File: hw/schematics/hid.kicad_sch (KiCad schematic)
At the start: 106 parts, among them M1 SK8701-01-004-SENSOR, SW1 SW_Push, SW10 SW_Push, SW11 SW_Push, SW12 SW_Push, SW13 SW_Push, SW14 SW_Push, SW15 SW_Push, SW16 SW_Push, SW17 SW_Push, SW18 SW_Push, SW19 SW_Push, SW2 SW_Push, SW20 SW_Push, SW21 SW_Push, SW22 SW_Push, SW23 SW_Push, SW3 SW_Push, SW4 SW_Push, SW5 SW_Push, SW6 SW_Push, SW7 SW_Push, SW8 SW_Push, SW9 SW_Push, U3 ADS122S14

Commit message: Hook up matrix
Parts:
- removed M1, rM1: SK8701-01-004-SENSOR, Alidade:SK8707-01-SENSOR, symbol Alidade:SK8701-01-004-SENSOR
- added M1, rM2: SK8701-01-005-SENSOR, Alidade:SK8707-01-005-SENSOR, symbol Alidade:SK8701-01-005-SENSOR
- added R6, R7, R8, R9, rR6, rR7, rR8, rR9: 10k, symbol Alidade:R
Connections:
- net 1V8: now also R6.1, R7.1, R8.1, R9.1
- net AIN0: now also M1.B
- net AIN1: now also M1.A
- net REFN: now also M1.D
- net REFP: now also M1.C
- net r1V8: now also rR6.1, rR7.1, rR8.1, rR9.1
- net rAIN0: now also rM2.B
- net rAIN1: now also rM2.A
- net rREFN: now also rM2.D
- net rREFP: now also rM2.C
- net rCOL2: now reaches rD1.3 (K), rD2.3 (K), rD3.3 (K), rD4.3 (K)
- net rROW2: now reaches rSW11.1, rSW14.1, rSW17.1, rSW20.1, rSW22.2, rSW3.1, rSW6.1
- net rROW2: now also rR7.2
- net COL3: now reaches D5.3 (K), D6.3 (K), D7.3 (K), D8.3 (K)
- net rROW1: now reaches rSW12.1, rSW13.1, rSW18.1, rSW19.1, rSW4.1, rSW5.1
- net rROW1: now also rR6.2
- net ROW3: now reaches SW10.1, SW15.1, SW16.1, SW2.1, SW21.1, SW23.2, SW7.1
- net ROW3: now also R8.2
- net COL6: now reaches D16.3 (K), D17.3 (K), D18.3 (K)
- net COL5: now reaches D13.3 (K), D14.3 (K), D15.3 (K)
- net rCOL6: now reaches rD16.3 (K), rD17.3 (K), rD18.3 (K)
- net rCOL7: now reaches rD19.3 (K), rD20.3 (K), rD21.3 (K)
- net ROW4: now reaches SW1.1, SW8.1, SW9.1
- net ROW4: now also R9.2
- net rCOL3: now reaches rD5.3 (K), rD6.3 (K), rD7.3 (K), rD8.3 (K)
- net rCOL5: now reaches rD13.3 (K), rD14.3 (K), rD15.3 (K)
- net rROW3: now reaches rSW10.1, rSW15.1, rSW16.1, rSW2.1, rSW21.1, rSW23.2, rSW7.1
- net rROW3: now also rR8.2
- net ROW1: now reaches SW12.1, SW13.1, SW18.1, SW19.1, SW4.1, SW5.1
- net ROW1: now also R6.2
- net rCOL4: now reaches rD10.3 (K), rD11.3 (K), rD12.3 (K), rD9.3 (K)
- net rROW4: now reaches rSW1.1, rSW8.1, rSW9.1
- net rROW4: now also rR9.2
- net COL2: now reaches D1.3 (K), D2.3 (K), D3.3 (K), D4.3 (K)
- net ROW2: now reaches SW11.1, SW14.1, SW17.1, SW20.1, SW22.2, SW3.1, SW6.1
- net ROW2: now also R7.2
- net COL1: now reaches D22.3 (K), D23.3 (K)
- net COL4: now reaches D10.3 (K), D11.3 (K), D12.3 (K), D9.3 (K)
- net COL7: now reaches D19.3 (K), D20.3 (K), D21.3 (K)
- net rCOL1: now reaches rD22.3 (K), rD23.3 (K)
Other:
- note added: "To scan the matrix: - Pull row low - Read column"
- note removed: "To scan the matrix: - Pull column low - Read row nibble"

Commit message: Annotate; Remove unused LDO/LS; Add RGB LED to PMIC
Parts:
- renumbered C12 to C10, C13 to C9, R3 to R10, R5 to R11, rC15 to rC10, rC13 to rC9, rR3 to rR10, rR5 to rR11
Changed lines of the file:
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@@
 		(on_board yes)
 		(dnp no)
-		(property "Reference" "rC15"
+		(property "Reference" "rC10"
 			(at 159.766 217.678 0)
 			(effects
@@
 			(project "alidade"
 				(path "/4cc5d416-57f5-4147-8183-e03ae6b1198a/2e72dd0e-817e-4022-b409-1f79b0de6857"
-					(reference "rC15")
+					(reference "rC10")
 					(unit 1)
 				)
@@
 		(on_board yes)
 		(dnp no)
-		(property "Reference" "C12"
+		(property "Reference" "C10"
 			(at 35.306 215.138 0)
 			(effects
@@
 			(project "alidade"
 				(path "/4cc5d416-57f5-4147-8183-e03ae6b1198a/2e72dd0e-817e-4022-b409-1f79b0de6857"
-					(reference "C12")
+					(reference "C10")
 					(unit 1)
 				)
@@
 		(on_board yes)
 		(dnp no)
-		(property "Reference" "rC13"
+		(property "Reference" "rC9"
 			(at 150.876 217.678 0)
 			(effects
@@
 			(project "alidade"
 				(path "/4cc5d416-57f5-4147-8183-e03ae6b1198a/2e72dd0e-817e-4022-b409-1f79b0de6857"
-					(reference "rC13")
+					(reference "rC9")
 					(unit 1)
 				)
@@
 		(on_board yes)
 		(dnp no)
-		(property "Reference" "R3"
+		(property "Reference" "R10"
 			(at 77.724 246.38 0)
 			(effects
@@
 			(project ""
 				(path "/4cc5d416-57f5-4147-8183-e03ae6b1198a/2e72dd0e-817e-4022-b409-1f79b0de6857"
-					(reference "R3")
+					(reference "R10")
 					(unit 1)
 				)
@@
 		(on_board yes)
 		(dnp no)
-		(property "Reference" "rR3"
+		(property "Reference" "rR10"
 			(at 202.184 248.92 0)
 			(effects
@@
 			(project "alidade"
 				(path "/4cc5d416-57f5-4147-8183-e03ae6b1198a/2e72dd0e-817e-4022-b409-1f79b0de6857"
-					(reference "rR3")
+					(reference "rR10")
 					(unit 1)
 				)
@@
 		(on_board yes)
 		(dnp no)
-		(property "Reference" "C13"
+		(property "Reference" "C9"
 			(at 26.416 215.138 0)
 			(effects
@@
 			(project "alidade"
 				(path "/4cc5d416-57f5-4147-8183-e03ae6b1198a/2e72dd0e-817e-4022-b409-1f79b0de6857"
-					(reference "C13")
+					(reference "C9")
 					(unit 1)
 				)
@@
 		(on_board yes)
 		(dnp no)
-		(property "Reference" "R5"
+		(property "Reference" "R11"
 			(at 77.724 254 0)
 			(effects
@@
 			(project "alidade"
 				(path "/4cc5d416-57f5-4147-8183-e03ae6b1198a/2e72dd0e-817e-4022-b409-1f79b0de6857"
-					(reference "R5")
+					(reference "R11")
 					(unit 1)
 				)
@@
 		(on_board yes)
 		(dnp no)
-		(property "Reference" "rR5"
+		(property "Reference" "rR11"
 			(at 202.184 256.54 0)
 			(effects
@@
 			(project "alidade"
 				(path "/4cc5d416-57f5-4147-8183-e03ae6b1198a/2e72dd0e-817e-4022-b409-1f79b0de6857"
-					(reference "rR5")
+					(reference "rR11")
 					(unit 1)
 				)

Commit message: Place shphld switches
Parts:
- added SW24, rSW24: SW_Push, symbol Alidade:SW_Push
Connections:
- net GND: now also SW24.2
- net rGND: now also rSW24.2
- new net SHPHLD: SW24.1
- new net rSHPHLD: rSW24.1
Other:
- note added: "SHPHLD Switches"

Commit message: Rename power rails
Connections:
- net 1V8 renamed DVDD
- net 3V3 renamed AVDD
- net r1V8 renamed rDVDD
- net r3V3 renamed rAVDD
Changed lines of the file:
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@@
 	)
 	(symbol
-		(lib_id "Alidade:1V8")
+		(lib_id "Alidade:DVDD")
 		(at 46.99 68.58 0)
 		(unit 1)
@@
 		(dnp no)
 		(fields_autoplaced yes)
-		(property "Reference" "#1V8_011"
+		(property "Reference" "#DVDD0106"
 			(at 46.99 72.39 0)
 			(effects
@@
 			)
 		)
-		(property "Value" "1V8"
+		(property "Value" "DVDD"
 			(at 46.99 63.5 0)
 			(effects
@@
 			(project "alidade"
 				(path "/4cc5d416-57f5-4147-8183-e03ae6b1198a/2e72dd0e-817e-4022-b409-1f79b0de6857"
-					(reference "#1V8_011")
+					(reference "#DVDD0106")
 					(unit 1)
 				)
@@
 	)
 	(symbol
-		(lib_id "Alidade:r3V3")
+		(lib_id "Alidade:rAVDD")
 		(at 158.75 207.01 0)
 		(unit 1)
@@
 		(dnp no)
 		(fields_autoplaced yes)
-		(property "Reference" "#r3V3_02"
+		(property "Reference" "#rAVDD0102"
 			(at 158.75 210.82 0)
 			(effects
@@
 			)
 		)
-		(property "Value" "r3V3"
+		(property "Value" "rAVDD"
 			(at 158.75 201.93 0)
 			(effects
@@
 			(project ""
 				(path "/4cc5d416-57f5-4147-8183-e03ae6b1198a/2e72dd0e-817e-4022-b409-1f79b0de6857"
-					(reference "#r3V3_02")
+					(reference "#rAVDD0102")
 					(unit 1)
 				)
@@
 	)
 	(symbol
-		(lib_id "Alidade:r1V8")
+		(lib_id "Alidade:rDVDD")
 		(at 374.65 99.06 0)
 		(unit 1)
@@
 		(dnp no)
 		(fields_autoplaced yes)
-		(property "Reference" "#r1V8_09"
+		(property "Reference" "#rDVDD0106"
 			(at 374.65 102.87 0)
 			(effects
@@
 			)
 		)
-		(property "Value" "r1V8"
+		(property "Value" "rDVDD"
 			(at 374.65 93.98 0)
 			(effects
@@
 			(project "alidade"
 				(path "/4cc5d416-57f5-4147-8183-e03ae6b1198a/2e72dd0e-817e-4022-b409-1f79b0de6857"
-					(reference "#r1V8_09")
+					(reference "#rDVDD0106")
 					(unit 1)
 				)
@@
 	)
 	(symbol
-		(lib_id "Alidade:r1V8")
+		(lib_id "Alidade:rDVDD")
 		(at 374.65 114.3 0)
 		(unit 1)
@@
 		(dnp no)
 		(fields_autoplaced yes)
-		(property "Reference" "#r1V8_05"
+		(property "Reference" "#rDVDD0107"
 			(at 374.65 118.11 0)
 			(effects
@@
 			)
 		)
-		(property "Value" "r1V8"
+		(property "Value" "rDVDD"
 			(at 374.65 109.22 0)
 			(effects
@@
 			(project "alidade"
 				(path "/4cc5d416-57f5-4147-8183-e03ae6b1198a/2e72dd0e-817e-4022-b409-1f79b0de6857"
-					(reference "#r1V8_05")
+					(reference "#rDVDD0107")
 					(unit 1)
 				)
@@
 	)
 	(symbol
-		(lib_id "Alidade:3V3")
+		(lib_id "Alidade:AVDD")
 		(at 34.29 204.47 0)
 		(unit 1)
@@
 		(dnp no)
 		(fields_autoplaced yes)
-		(property "Reference" "#3V3_02"
+		(property "Reference" "#AVDD0102"
 			(at 34.29 208.28 0)
 			(effects
@@
 			)
 		)
-		(property "Value" "3V3"
+		(property "Value" "AVDD"
 			(at 34.29 199.39 0)
 			(effects
@@
 			(project ""
 				(path "/4cc5d416-57f5-4147-8183-e03ae6b1198a/2e72dd0e-817e-4022-b409-1f79b0de6857"
-					(reference "#3V3_02")
+					(reference "#AVDD0102")
 					(unit 1)
 				)
@@
 	)
 	(symbol
-		(lib_id "Alidade:1V8")
+		(lib_id "Alidade:DVDD")
 		(at 46.99 83.82 0)
 		(unit 1)
@@
 		(dnp no)
 		(fields_autoplaced yes)
-		(property "Reference" "#1V8_010"
+		(property "Reference" "#DVDD0107"
 			(at 46.99 87.63 0)
 			(effects
@@
 			)
 		)
-		(property "Value" "1V8"
+		(property "Value" "DVDD"
 			(at 46.99 78.74 0)
 			(effects
@@
 			(project "alidade"
 				(path "/4cc5d416-57f5-4147-8183-e03ae6b1198a/2e72dd0e-817e-4022-b409-1f79b0de6857"
-					(reference "#1V8_010")
+					(reference "#DVDD0107")
 					(unit 1)
 				)
@@
 	)
 	(symbol
-		(lib_id "Alidade:1V8")
+		(lib_id "Alidade:DVDD")
 		(at 25.4 204.47 0)
 		(unit 1)
@@
 		(dnp no)
 		(fields_autoplaced yes)
-		(property "Reference" "#1V8_06"
+		(property "Reference" "#DVDD0104"
 			(at 25.4 208.28 0)
 			(effects
@@
 			)
 		)
-		(property "Value" "1V8"
+		(property "Value" "DVDD"
 			(at 25.4 199.39 0)
 			(effects
@@
 			(project ""
 				(path "/4cc5d416-57f5-4147-8183-e03ae6b1198a/2e72dd0e-817e-4022-b409-1f79b0de6857"
-					(reference "#1V8_06")
+					(reference "#DVDD0104")
 					(unit 1)
 				)
@@
 	)
 	(symbol
-		(lib_id "Alidade:1V8")
+		(lib_id "Alidade:DVDD")
 		(at 46.99 114.3 0)
 		(unit 1)
@@
 		(dnp no)
 		(fields_autoplaced yes)
-		(property "Reference" "#1V8_04"
+		(property "Reference" "#DVDD0105"
 			(at 46.99 118.11 0)
 			(effects
@@
 			)
 		)
-		(property "Value" "1V8"
+		(property "Value" "DVDD"
 			(at 46.99 109.22 0)
 			(effects
@@
 			(project "alidade"
 				(path "/4cc5d416-57f5-4147-8183-e03ae6b1198a/2e72dd0e-817e-4022-b409-1f79b0de6857"
-					(reference "#1V8_04")
+					(reference "#DVDD0105")
 					(unit 1)
 				)
@@
 	)
 	(symbol
-		(lib_id "Alidade:r1V8")
+		(lib_id "Alidade:rDVDD")
 		(at 374.65 68.58 0)
 		(unit 1)
@@
 		(dnp no)
 		(fields_autoplaced yes)
-		(property "Reference" "#r1V8_011"
+		(property "Reference" "#rDVDD0105"
 			(at 374.65 72.39 0)
 			(effects
@@
 			)
 		)
-		(property "Value" "r1V8"
+		(property "Value" "rDVDD"
 			(at 374.65 63.5 0)
 			(effects
@@
 			(project "alidade"
 				(path "/4cc5d416-57f5-4147-8183-e03ae6b1198a/2e72dd0e-817e-4022-b409-1f79b0de6857"
-					(reference "#r1V8_011")
+					(reference "#rDVDD0105")
 					(unit 1)
 				)
@@
 	)
 	(symbol
-		(lib_id "Alidade:r1V8")
+		(lib_id "Alidade:rDVDD")
 		(at 374.65 83.82 0)
 		(unit 1)
@@
 		(dnp no)
 		(fields_autoplaced yes)
-		(property "Reference" "#r1V8_010"
+		(property "Reference" "#rDVDD0104"
 			(at 374.65 87.63 0)
 			(effects
@@
 			)
 		)
-		(property "Value" "r1V8"
+		(property "Value" "rDVDD"
 			(at 374.65 78.74 0)
 			(effects
@@
 			(project "alidade"
 				(path "/4cc5d416-57f5-4147-8183-e03ae6b1198a/2e72dd0e-817e-4022-b409-1f79b0de6857"
-					(reference "#r1V8_010")
+					(reference "#rDVDD0104")
 					(unit 1)
 				)
@@
 	)
 	(symbol
-		(lib_id "Alidade:r1V8")
+		(lib_id "Alidade:rDVDD")
 		(at 149.86 207.01 0)
 		(unit 1)
@@
 		(dnp no)
 		(fields_autoplaced yes)
-		(property "Reference" "#r1V8_04"
+		(property "Reference" "#rDVDD0103"
 			(at 149.86 210.82 0)
 			(effects
@@
 			)
 		)
-		(property "Value" "r1V8"
+		(property "Value" "rDVDD"
 			(at 149.86 201.93 0)
 			(effects
@@
 			(project ""
 				(path "/4cc5d416-57f5-4147-8183-e03ae6b1198a/2e72dd0e-817e-4022-b409-1f79b0de6857"
-					(reference "#r1V8_04")
+					(reference "#rDVDD0103")
 					(unit 1)
 				)
@@
 	)
 	(symbol
-		(lib_id "Alidade:1V8")
+		(lib_id "Alidade:DVDD")
 		(at 46.99 99.06 0)
 		(unit 1)
@@
 		(dnp no)
 		(fields_autoplaced yes)
-		(property "Reference" "#1V8_09"
+		(property "Reference" "#DVDD0103"
 			(at 46.99 102.87 0)
 			(effects
@@
 			)
 		)
-		(property "Value" "1V8"
+		(property "Value" "DVDD"
 			(at 46.99 93.98 0)
 			(effects
@@
 			(project "alidade"
 				(path "/4cc5d416-57f5-4147-8183-e03ae6b1198a/2e72dd0e-817e-4022-b409-1f79b0de6857"
-					(reference "#1V8_09")
+					(reference "#DVDD0103")
 					(unit 1)
 				)

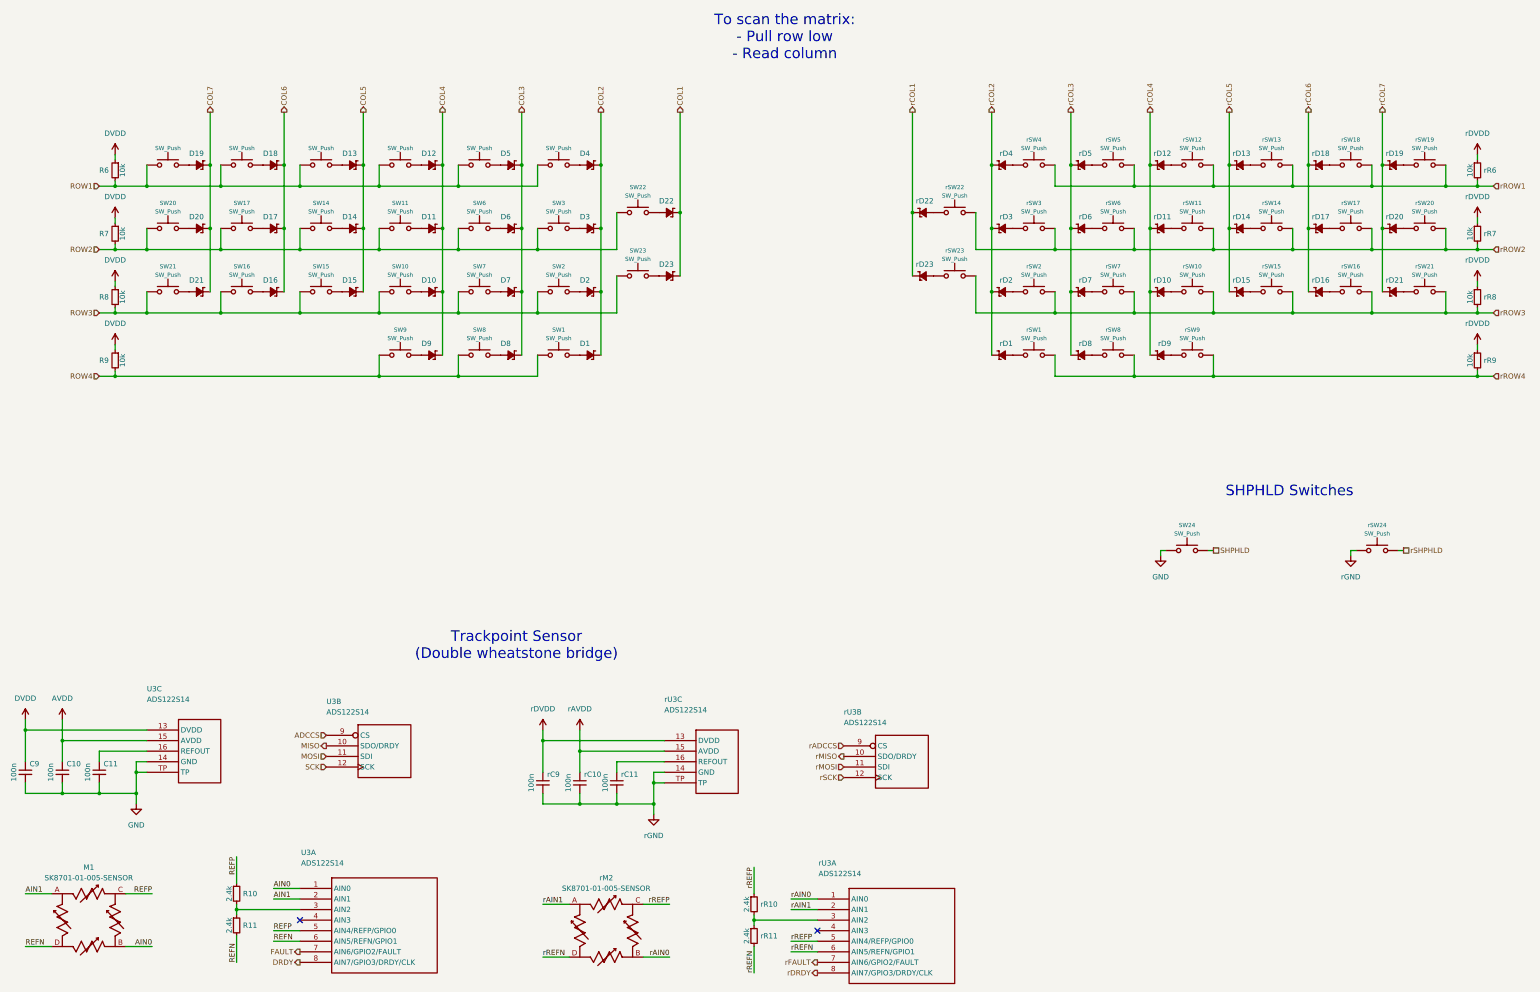
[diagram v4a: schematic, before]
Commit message: Use new switch for shphld
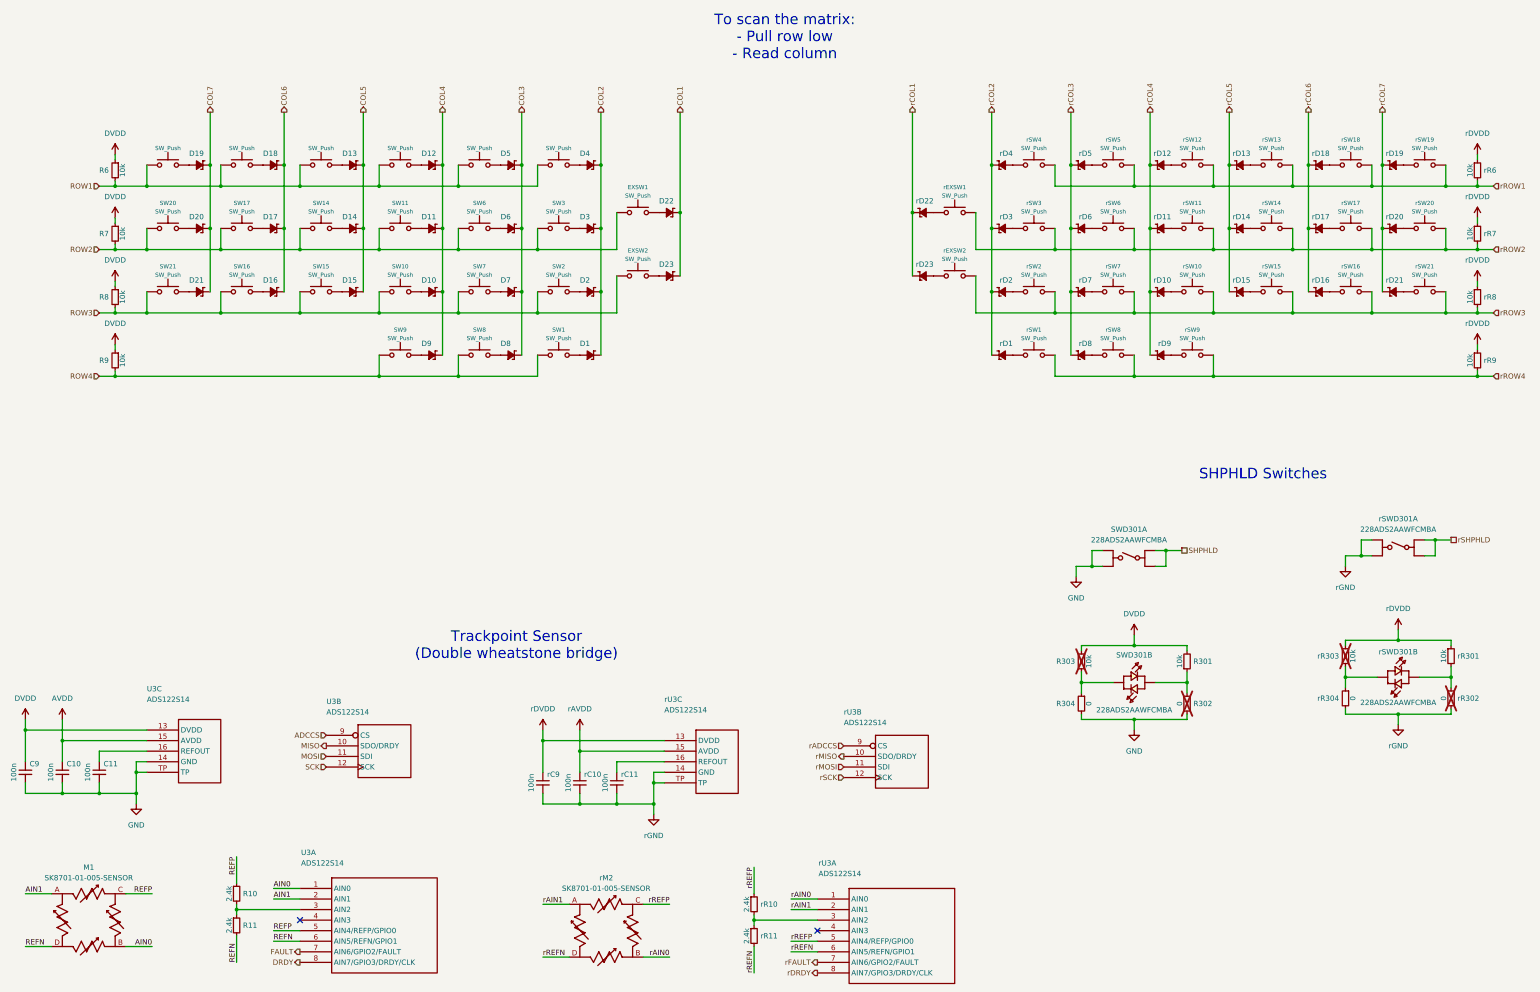
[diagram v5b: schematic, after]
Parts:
- removed SW24, rSW24: SW_Push, symbol Alidade:SW_Push
- added R301, R303, rR301, rR303: 10k, Alidade:0603, symbol Alidade:R
- added R302, R304, rR302, rR304: 0, Alidade:0603, symbol Alidade:R
- added SWD301, rSWD301: 228ADS2AAWFCMBA, symbol Alidade:228A
- C10, C11, C9, R10, R11, R6, R7, R8, R9, rC10, rC11, rC9, rR10, rR11, rR6, rR7, rR8, rR9: footprint (none) -> Alidade:0603
- U3, rU3: footprint (none) -> Alidade:RTE0016C-MFG
- renumbered SW22 to EXSW1, SW23 to EXSW2, rSW22 to rEXSW1, rSW23 to rEXSW2
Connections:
- net DVDD: now also R301.2, R303.1
- net GND: now also R302.1, R304.2, SWD301.1, SWD301.2
- net SHPHLD: now also SWD301.3, SWD301.4
- net rDVDD: now also rR301.1, rR303.1
- net rGND: now also rR302.2, rR304.2, rSWD301.1, rSWD301.2
- net rSHPHLD: now also rSWD301.3, rSWD301.4
- new net: rR303.2, rR304.1, rSWD301.L1
- new net: R301.1, R302.2, SWD301.L2
- new net: R303.2, R304.1, SWD301.L1
- new net: rR301.2, rR302.1, rSWD301.L2
